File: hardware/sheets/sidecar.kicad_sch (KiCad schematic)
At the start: 3 parts, among them J1 ISA 8-bit (60p)

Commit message: JLCPCB sourcing pass: verify pinouts, LCSC part numbers, SMD build
Custom-symbol verification (open-questions Q5 resolved):
- MAX3241 symbol was wrong on nearly every pin and used MAX3243-style
  control names; regenerated to the real SSOP-28 pinout (SHDN#/EN#/
  R1OUTB/R2OUTB) and com_port rewired -- EN# must be GROUNDED (the old
  ~FORCEON-high would have disabled the receivers on real silicon)
- DS12C887 symbol wrong on 4 pins (DS=17, RESET#=18, IRQ#=19, SQW=23)

Sourcing (every part checked against the JLC DB; ~45 line items):
- New tools/parts.py maps (lib_id, value) -> LCSC; build.py applies it as
  an 'LCSC Part Num' property on every component (384 across the project)
- Sheets stay generic; stock-forced substitutions bound in the map:
  '374->'574 (parallel rewired), '163->'161, '157->HC157 (+HCT-buffered
  3.3V selects, I0/I1 swapped), '02->HC02, TCM809->MCP809, 2N3904->MMBT3904
- bus_mcu address counters moved to the 3.3V domain (HC161 on 3V3_BUS,
  loaded from MCU-side MD0-7; HCT244s read the 3.3V outputs at TTL Vih)
- 14.318 XOs are 3.3V-only parts: powered from 3V3, squared up via spare
  HCT gates (cpu_core U13, card_isatest U19)
- COM baud reference is now a 1.8432MHz crystal on the 16C550's XIN/XOUT
  (3.3V-only oscillators vs a 5V-only soft card)
- Supervisor QSPI header replaced with a real W25Q128JVSIQ
- Socket policy (fab installs sockets): V20 DIP-40, SRAM DIP-32 (no 5V
  512Kx8 SRAM at JLC at all), DS12C887 DIP-24, female headers for modules

Docs: CLAUDE.md fabrication-constraints section (SMD, 100x100mm, generic-
symbols rule, voltage-domain rule); README + hardware/README fab notes;
notes/jlcpcb-sourcing.md (decisions, thin-stock flags, not-at-JLC list);
stale questions-sidecar.md collapsed to its supersession record.

Rebuilt motherboard + cards: structural ERC 0, byte-identical rebuilds.

Co-Authored-By: Claude Fable 5 <noreply@anthropic.com>
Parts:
- C1, C2: LCSC Part Num (none) -> C14663
- J1: LCSC Part Num (none) -> C2333
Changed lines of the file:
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@@
+			)
+		)
+		(property "LCSC Part Num" "C2333"
+			(at 177.8 152.4 0)
+			(effects
+				(font
+					(size 1.27 1.27)
+				)
+				(hide yes)
 			)
 		)
@@
 			)
 		)
+		(property "LCSC Part Num" "C14663"
+			(at 205.74 134.62 0)
+			(effects
+				(font
+					(size 1.27 1.27)
+				)
+				(hide yes)
+			)
+		)
 		(pin "1"
 		)
@@
 			(at 218.44 134.62 0)
 			(effects
+				(font
+					(size 1.27 1.27)
+				)
+				(hide yes)
+			)
+		)
+		(property "LCSC Part Num" "C14663"
+			(at 218.44 134.62 0)
+			(effects

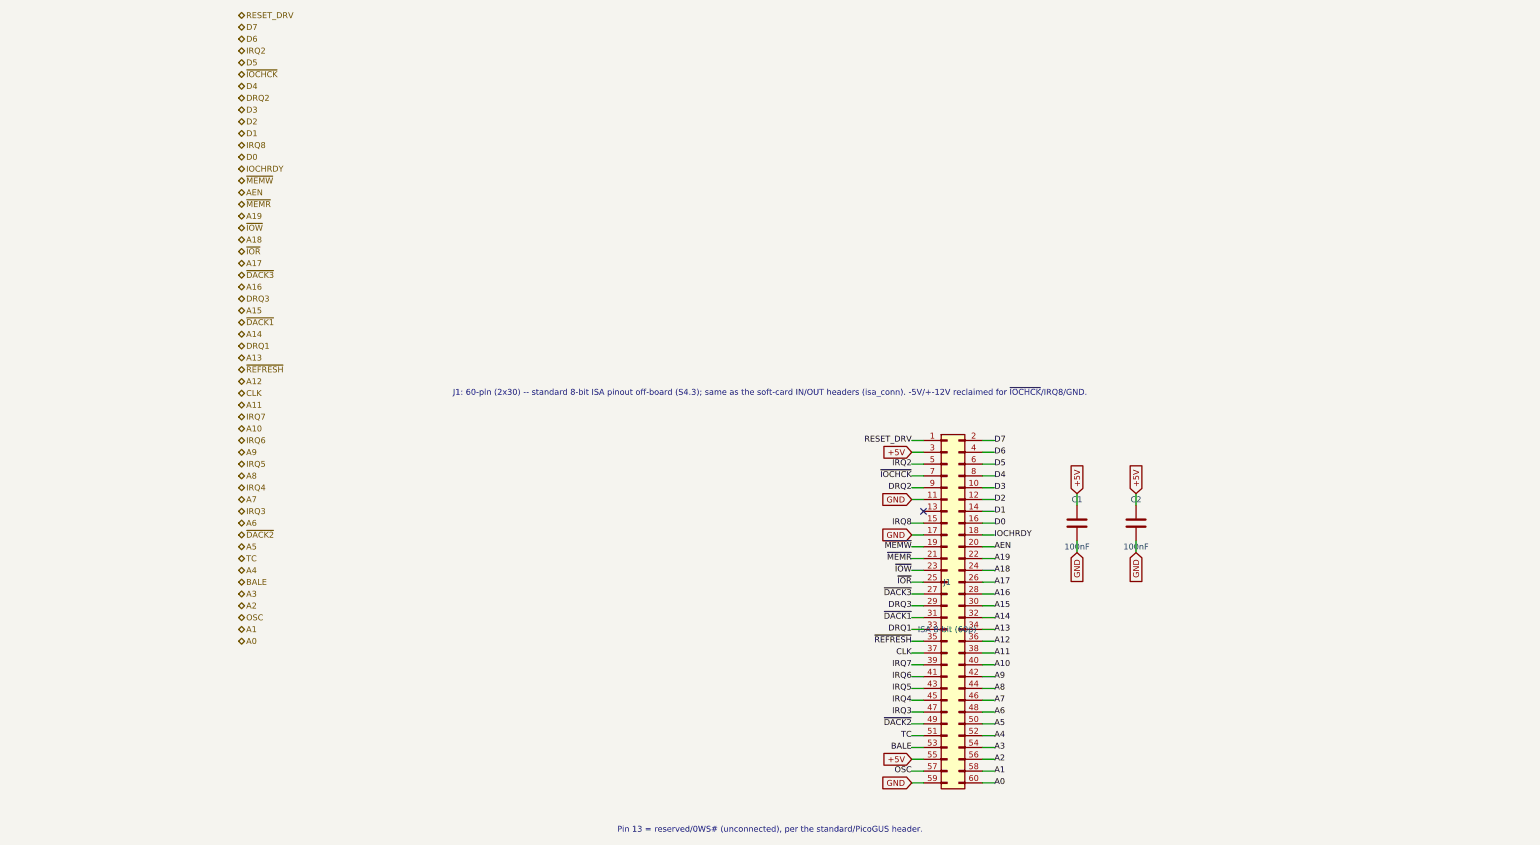
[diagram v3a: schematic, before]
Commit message: Design review 2026-07-11: rail protection, decoupling, wiring fixes
Protection:
- Sidecar +5V now feeds through a 2A polyfuse into +5V_ISA with an
  SMBJ5.0A clamp + 22uF bulk (a faulted ISA card trips its own fuse
  instead of dropping the board; back-fed voltage is clamped).
- USB-C VBUS enters through a 3A polyfuse with an SMBJ5.0A on +5V
  (backstop for the CFG1 9-20V failure mode). CH224K gains a 1uF VDD
  cap; its PG routes to Supervisor GPIO16 as PD_PG. Buck output
  doubled to 2x22uF, 10uF at VIN, extra rail bulk.
- Supervisor USB-A host port: 27R series termination (RP2040
  requirement), USBLC6-2SC6 ESD array, 100uF VBUS bulk.
- Video: HDMI +5V fused (500mA), HPD sensed on GPIO41, 100R series on
  VGA sync. TMDS ESD array deferred to layout (no symbol).
- card_isatest: V5RAW bulk, Q1 gate soft-start cap, TVS on DUT rail.

Wiring fixes:
- SPKR had no driver anywhere (netlist: 1 node). Bus MCU GPIO22
  reassigned from the diagnostics-only bus-CLK sense to SPKR; bus_mcu
  drops CLK from its interface. Doc 5.2 updated.
- bus_mcu C8 decoupled +3V3, a rail that sheet never uses -> 3V3_BUS.
- Storage IRQ5 was push-pull (permanently driven when idle) -> 2N7002
  + gated '125 tri-state, same convention as the LPT IRQ7 stage.
- MAX3241 pump caps resized to the 5V datasheet values (47nF/330nF).
- LPT DB25 status inputs get 4.7k pull-ups (floated with no printer).
- Audio line-out gets a 100R series isolator before the jack.

Best practices:
- Decoupling to ~1x100nF per IC on every sheet + bulk per board
  (cpu_core 7->16 incl. the naked 3.3V oscillator, storage 4->11,
  parallel 6->13, rtc/com/video/bus_mcu/card_isatest similar).
- All floating spare CMOS inputs tied ('00/'74/'157/'02/'04/'125
  sections across cpu_core, bus_mcu, rtc, storage, card_isatest).

Sourcing: new parts mapped in parts.py with JLC-verified LCSC numbers;
Power_Protection lib registered in the tools; TPS563200 stock alert
(4 pcs left at JLC) flagged in parts.py + jlcpcb-sourcing.md. All
decisi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
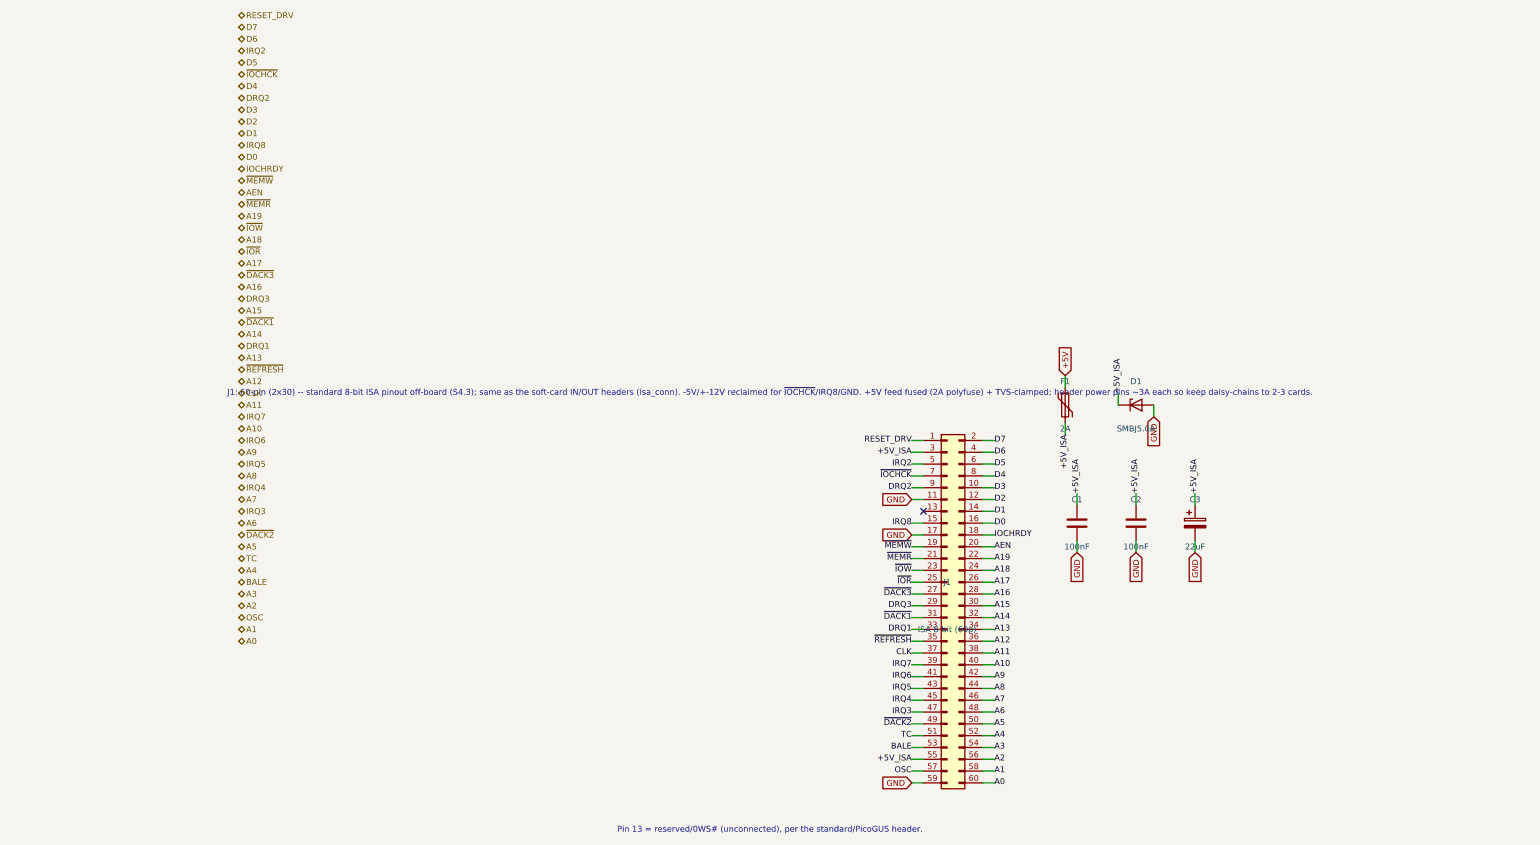
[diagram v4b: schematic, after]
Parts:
- added C1, C2: 100nF, symbol Device:C
- added C3: 22uF, symbol Device:C_Polarized
- D1: renamed from C2; value 100nF -> SMBJ5.0A; symbol Device:C -> Device:D_Zener; LCSC Part Num C14663 -> C19077558
- F1: renamed from C1; value 100nF -> 2A; symbol Device:C -> Device:Polyfuse; LCSC Part Num C14663 -> C883156
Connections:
- net +5V: no longer D1.1, J1.3 (Pin_3), J1.55 (Pin_55)
- net GND: now also C1.2, C2.2, C3.2; no longer F1.2
- new net +5V_ISA: C1.1, C2.1, C3.1, D1.1 (K), F1.2, J1.3 (Pin_3), J1.55 (Pin_55)
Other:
- note added: "J1: 60-pin (2x30) -- standard 8-bit ISA pinout off-board (S4.3); same as the soft-card IN/OUT headers (isa_conn). -5V/+-12V reclaimed for ~{IOCHCK}/IRQ8/GND. +5V feed fused (2A polyfuse) + TVS-clamped; header power pins ~3A each so keep daisy-chains to 2-3 cards."
- note removed: "J1: 60-pin (2x30) -- standard 8-bit ISA pinout off-board (S4.3); same as the soft-card IN/OUT headers (isa_conn). -5V/+-12V reclaimed for ~{IOCHCK}/IRQ8/GND."
